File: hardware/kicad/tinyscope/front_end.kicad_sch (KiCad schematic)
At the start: 0 parts

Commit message: feat: hardware: Adds first stage TVS diodes for Front End A/B
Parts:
- added D10, D11: SMAJ48CA, Diode_SMD:D_SMA, symbol Diode:SMAJ48CA
- added J6: Front End A, symbol Connector:Conn_Coaxial
- added J7: Front End B, symbol Connector:Conn_Coaxial
- added R? (x2): 1M, symbol Device:R_Small
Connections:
- new net: D11.2 (A2), J7.1 (In), R?.1
- new net: D10.2 (A2), J6.1 (In), R?.1
- new net GND: D10.1 (A1), D11.1 (A1), J6.2 (Ext), J7.2 (Ext), R?.2, R?.2

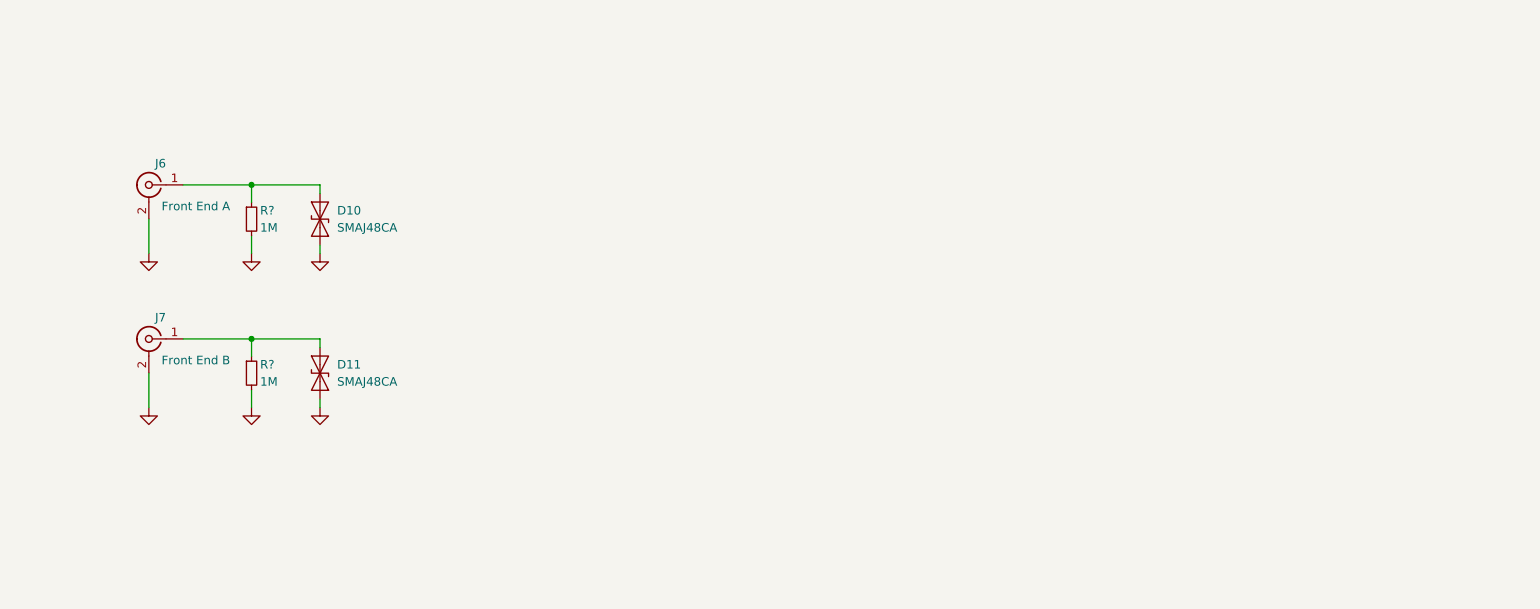
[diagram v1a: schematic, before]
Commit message: feat: hardware: Adds BV199 clamps and AD8065 buffers for Front End A/B
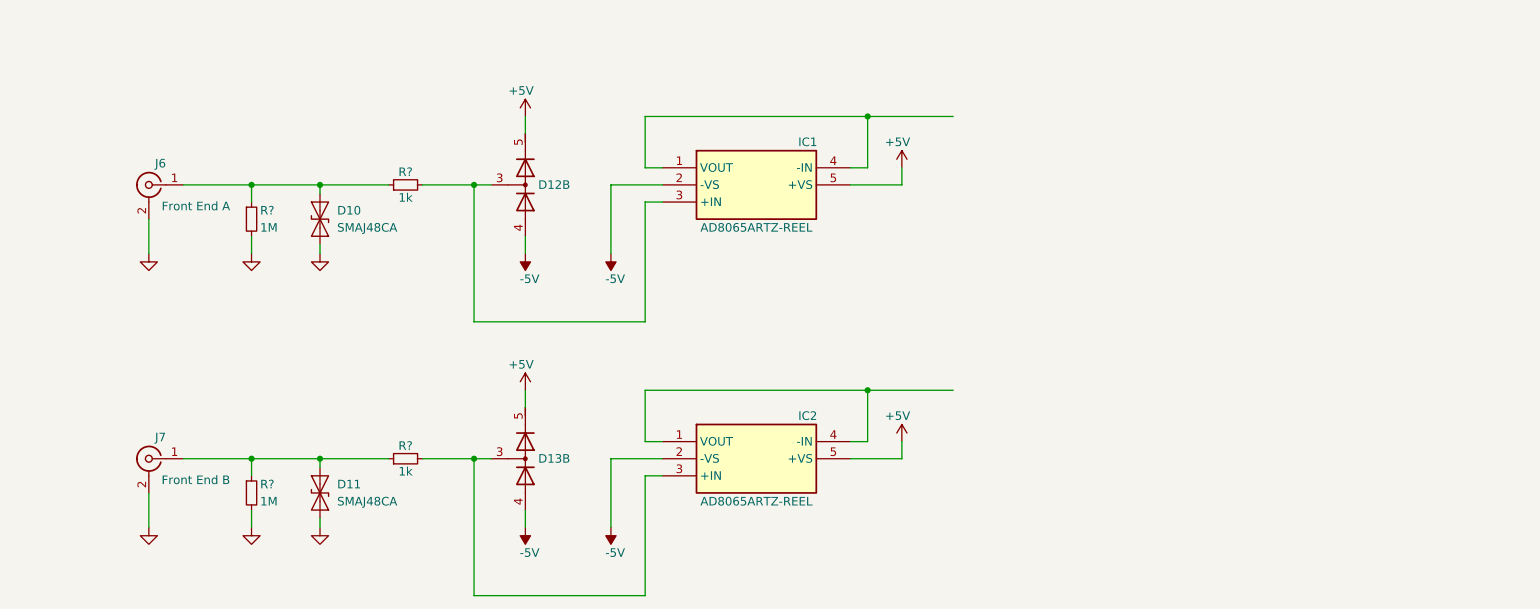
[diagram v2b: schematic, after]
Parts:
- added D12, D13: BAV199DW, Package_TO_SOT_SMD:SOT-363_SC-70-6, symbol Diode:BAV199DW
- added IC1, IC2: AD8065ARTZ-REEL, SOT95P280X145-5N, symbol AD8065ARTZ-REEL:AD8065ARTZ-REEL
- added R? (x2): 1k, symbol Device:R_Small
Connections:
- net at D11.2 (A2), J7.1 (In), R?.1: now also R?.1
- net at D10.2 (A2), J6.1 (In), R?.1: now also R?.1
- new net: D13.3 (K1A2), IC2.3 (+IN), R?.2
- new net: D12.3 (K1A2), IC1.3 (+IN), R?.2
- new net: IC1.1 (VOUT), IC1.4 (-IN)
- new net: IC2.1 (VOUT), IC2.4 (-IN)
- new net +5V: D12.5 (K4), D13.5 (K4), IC1.5 (+VS), IC2.5 (+VS)
- new net -5V: D12.4 (A3), D13.4 (A3), IC1.2 (-VS), IC2.2 (-VS)
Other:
- moved on the sheet: D11, J7, R?

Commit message: feat: hardware: Finishes front ends stage 4
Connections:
- net AD8065_VOUT: now reaches IC1.1 (VOUT), IC1.4 (-IN)
- net AD8065_VOUT: now also IC2.1 (VOUT), IC2.4 (-IN)
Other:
- moved on the sheet: D10, D11, D12B, D13B, IC1, IC2, J6, J7, R?

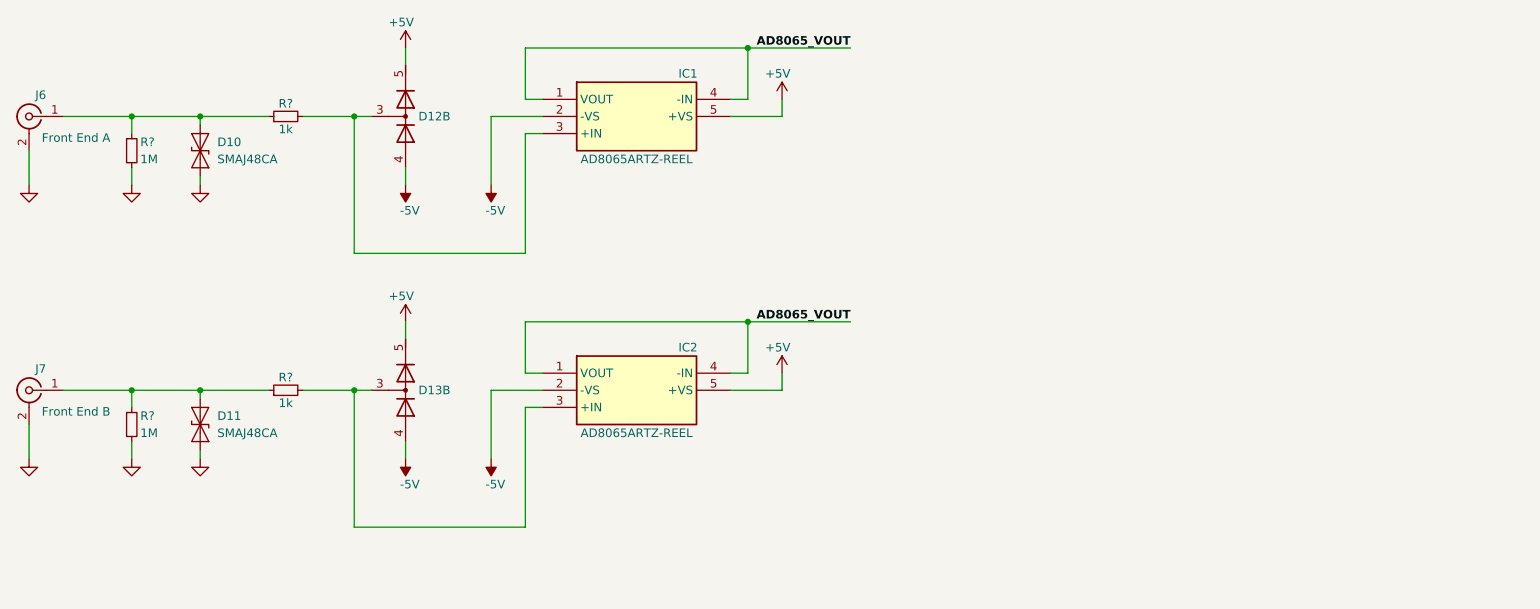
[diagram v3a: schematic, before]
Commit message: feat: hardware: Add front ends stage 5. Replaces AD8065 with AD8066
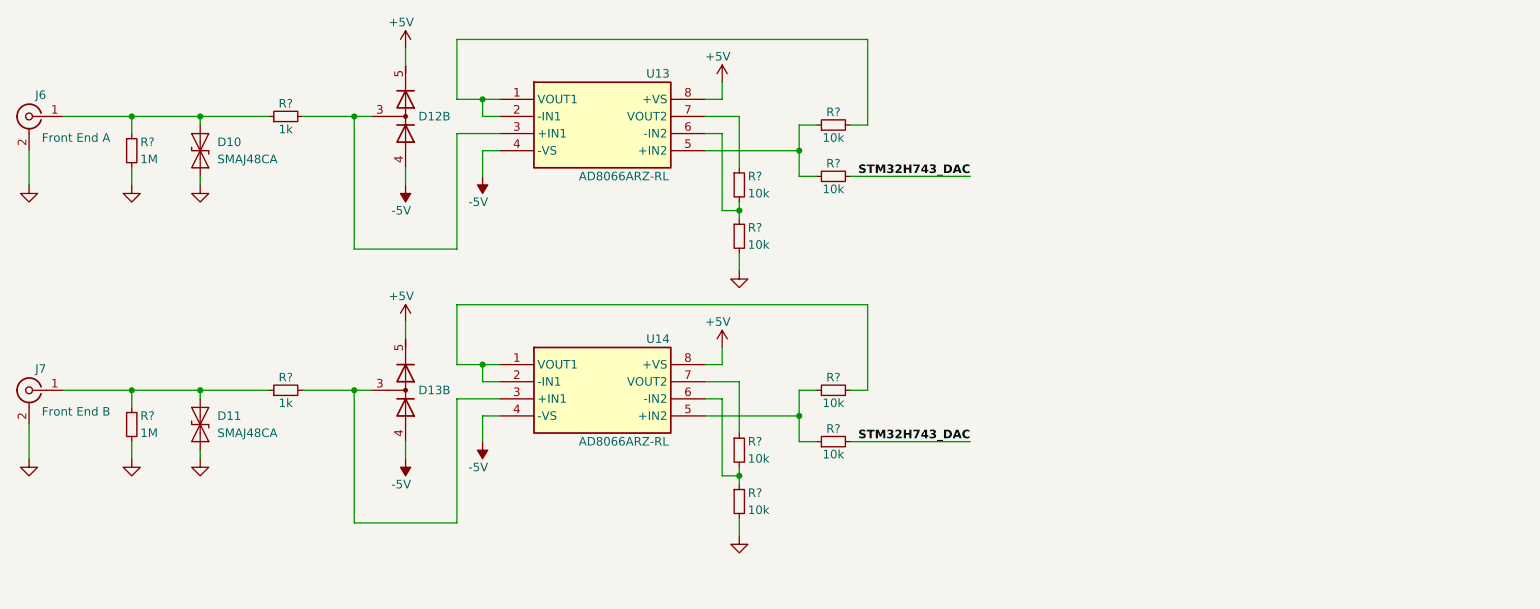
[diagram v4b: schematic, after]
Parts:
- removed IC1, IC2: AD8065ARTZ-REEL, SOT95P280X145-5N, symbol AD8065ARTZ-REEL:AD8065ARTZ-REEL
- added R? (x8): 10k, symbol Device:R_Small
- added U13, U14: AD8066ARZ-RL, SOIC127P600X175-8N, symbol AD8066ARZ-RL:AD8066ARZ-RL
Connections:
- net +5V: now also U13.8 (+VS), U14.8 (+VS)
- net -5V: now also U13.4 (-VS), U14.4 (-VS)
- net GND: now also R?.2, R?.2
- net at D13.3 (K1A2), R?.2: now also U14.3 (+IN1)
- net at D12.3 (K1A2), R?.2: now also U13.3 (+IN1)
- new net: R?.1, U13.7 (VOUT2)
- new net: R?.1, R?.2, U13.6 (-IN2)
- new net: R?.1, U14.7 (VOUT2)
- new net: R?.1, R?.2, U14.6 (-IN2)
- new net: R?.1, R?.1, U13.5 (+IN2)
- new net: R?.1, R?.1, U14.5 (+IN2)
- new net: R?.2, U14.1 (VOUT1), U14.2 (-IN1)
- new net: R?.2, U13.1 (VOUT1), U13.2 (-IN1)
- new net STM32H743_DAC: R?.2, R?.2

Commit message: feat: hardware: Switches SPI1 to SPI4. Adds DAC1_OUT1 and DAC1_OUT2
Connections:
- net STM32H743_DAC renamed STM32H743_DAC1_OUT1
- net STM32H743_DAC1_OUT1: no longer R?.2
- new net STM32H743_DAC1_OUT2: R?.2
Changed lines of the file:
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@@
     (stroke (width 0) (type default))
   )
-  (wire (pts (xy 147.32 39.37) (xy 165.1 39.37))
+  (wire (pts (xy 147.32 39.37) (xy 172.085 39.37))
     (stroke (width 0) (type default))
   )
@@
     (stroke (width 0) (type default))
   )
-  (wire (pts (xy 147.32 78.74) (xy 165.1 78.74))
+  (wire (pts (xy 147.32 78.74) (xy 172.085 78.74))
     (stroke (width 0) (type default))
   )
@@
     (stroke (width 0) (type default))
   )
-  (label "STM32H743_DAC" (at 165.1 39.37 180) (fields_autoplaced)
+  (label "STM32H743_DAC1_OUT1" (at 172.085 39.37 180) (fields_autoplaced)
     (effects (font (size 1.27 1.27) bold) (justify right bottom))
   )
-  (label "STM32H743_DAC" (at 165.1 78.74 180) (fields_autoplaced)
+  (label "STM32H743_DAC1_OUT2" (at 172.085 78.74 180) (fields_autoplaced)
     (effects (font (size 1.27 1.27) bold) (justify right bottom))
   )

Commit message: feat: hardware: note: Starts the desing of the Sallen and Key Low Pass Filter filter (anti-aliasing)
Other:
- note added: "Place for Sallen and Key Low Pass Filter"
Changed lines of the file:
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@@
   (junction (at 92.71 27.94) (diameter 0) (color 0 0 0 0)
   )
+  (junction (at 130.81 30.48) (diameter 0) (color 0 0 0 0)
+  )
   (junction (at 40.64 71.12) (diameter 0) (color 0 0 0 0)
   )
@@
   (junction (at 40.64 30.48) (diameter 0) (color 0 0 0 0)
   )
+  (junction (at 130.81 69.85) (diameter 0) (color 0 0 0 0)
+  )
   (junction (at 139.7 35.56) (diameter 0) (color 0 0 0 0)
   )
@@
     (stroke (width 0) (type default))
   )
+  (wire (pts (xy 130.81 67.31) (xy 172.085 67.31))
+    (stroke (width 0) (type default))
+  )
   (wire (pts (xy 130.81 90.17) (xy 130.81 92.71))
     (stroke (width 0) (type default))
@@
     (stroke (width 0) (type default))
   )
+  (wire (pts (xy 130.81 27.94) (xy 130.81 30.48))
+    (stroke (width 0) (type default))
+  )
   (wire (pts (xy 88.9 58.42) (xy 88.9 67.31))
     (stroke (width 0) (type default))
@@
     (stroke (width 0) (type default))
   )
+  (wire (pts (xy 130.81 67.31) (xy 130.81 69.85))
+    (stroke (width 0) (type default))
+  )
   (wire (pts (xy 142.24 71.12) (xy 139.7 71.12))
     (stroke (width 0) (type default))
@@
     (stroke (width 0) (type default))
   )
+  (wire (pts (xy 130.81 27.94) (xy 172.085 27.94))
+    (stroke (width 0) (type default))
+  )
   (wire (pts (xy 139.7 35.56) (xy 139.7 39.37))
     (stroke (width 0) (type default))
@@
     (stroke (width 0) (type default))
   )
+  (text "Place for Sallen and Key Low Pass Filter" (at 180.975 53.975 0)
+    (effects (font (size 1.27 1.27)) (justify left bottom))
+  )
   (label "STM32H743_DAC1_OUT1" (at 172.085 39.37 180) (fields_autoplaced)

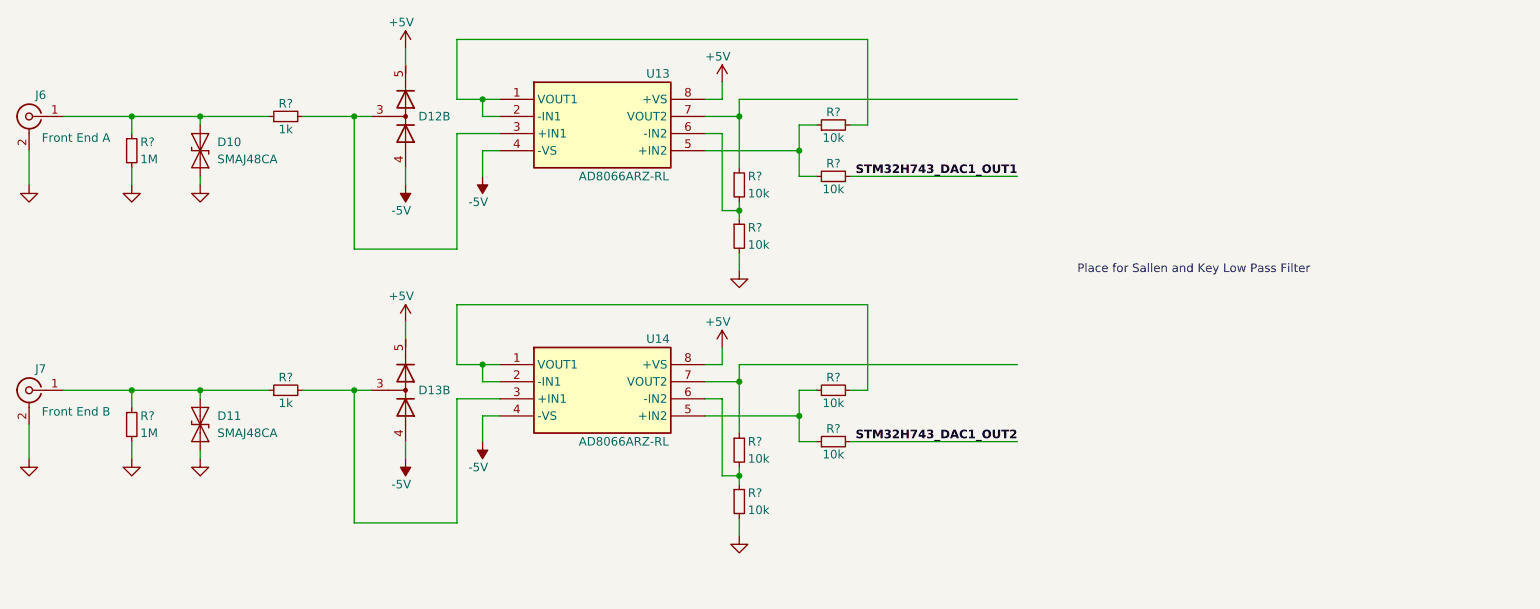
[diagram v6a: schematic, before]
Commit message: feat: hardware: note: Adds the two Sallen and Key Low Pass Filter filter (anti-aliasing) topologies
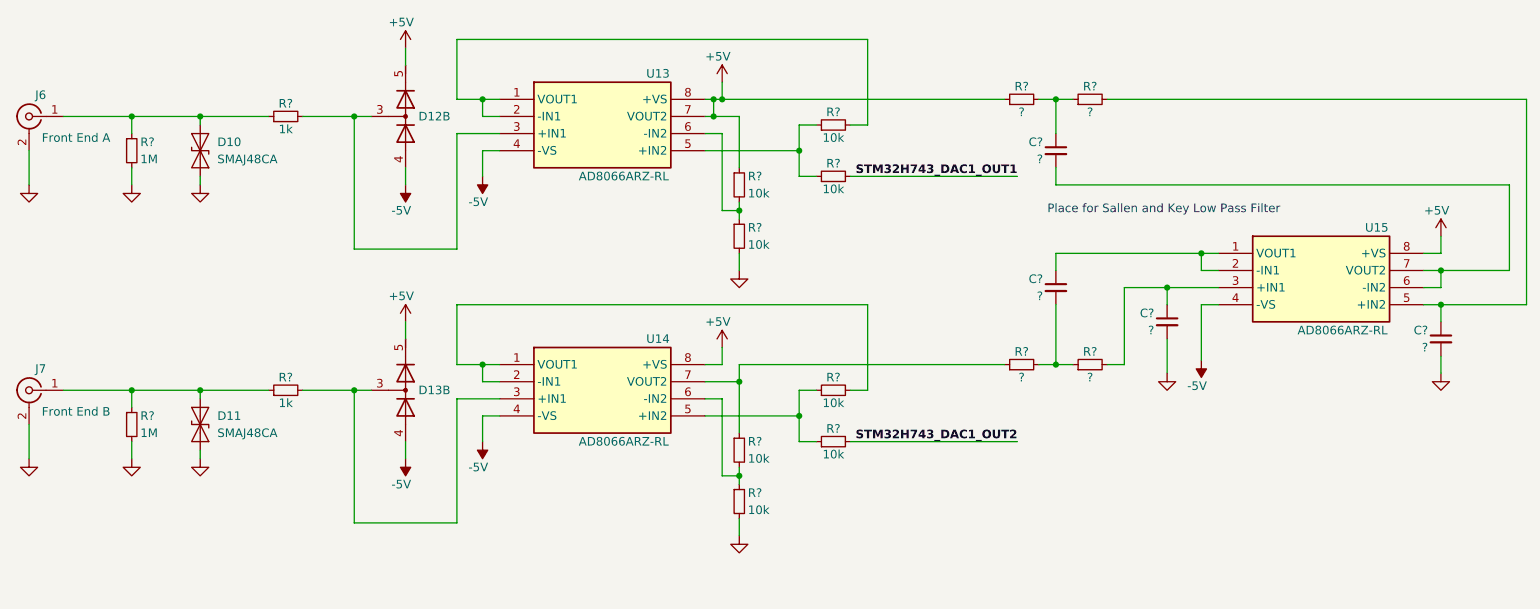
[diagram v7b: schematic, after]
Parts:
- added C? (x4): ?, symbol Device:C_Small
- added R? (x4): ?, symbol Device:R_Small
- added U15: AD8066ARZ-RL, SOIC127P600X175-8N, symbol AD8066ARZ-RL:AD8066ARZ-RL
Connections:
- net +5V: now also R?.1, U13.7 (VOUT2), R?.1, U15.8 (+VS)
- net -5V: now also U15.4 (-VS)
- net GND: now also C?.2, C?.2
- net at R?.1, U14.7 (VOUT2): now also R?.1
- new net: C?.1, R?.2, U15.5 (+IN2)
- new net: C?.1, R?.1, R?.2
- new net: C?.1, U15.1 (VOUT1), U15.2 (-IN1)
- new net: C?.1, R?.2, U15.3 (+IN1)
- new net: C?.2, U15.6 (-IN2), U15.7 (VOUT2)
- new net: C?.2, R?.1, R?.2

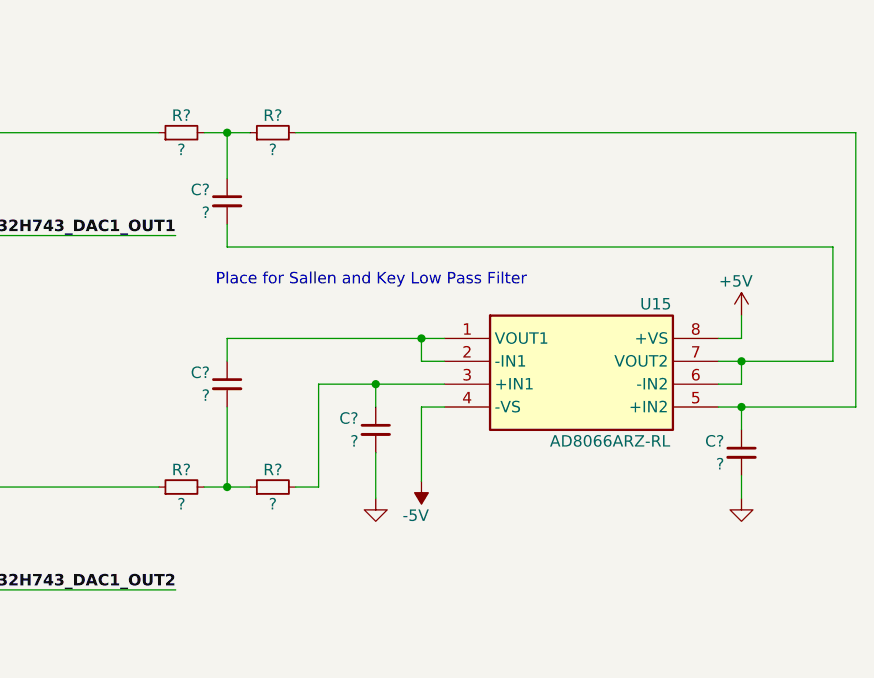
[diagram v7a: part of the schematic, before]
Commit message: feat: hardware: note: Adds the two Sallen and Key Low Pass Filter filter (anti-aliasing) parts values
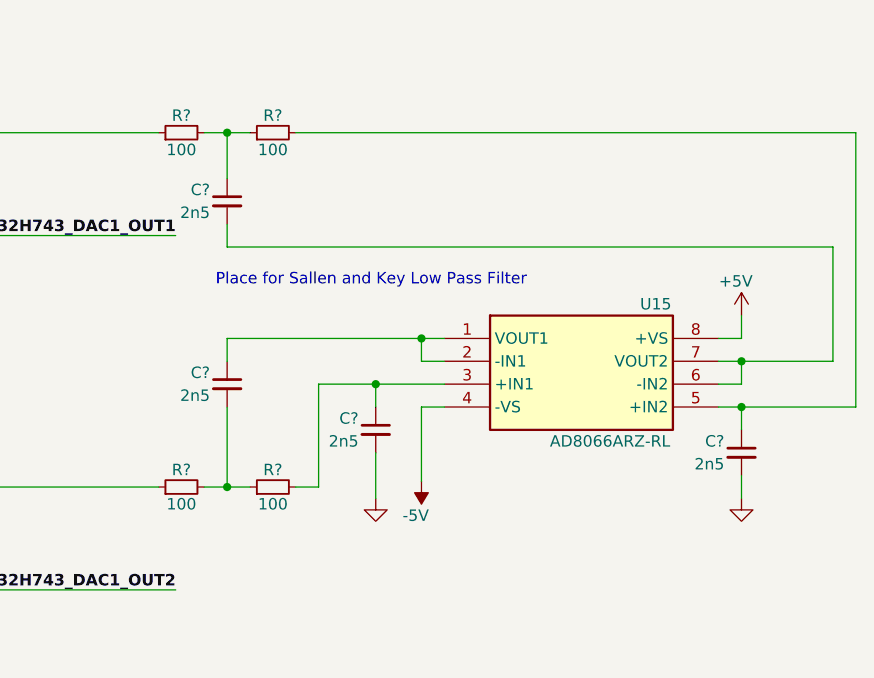
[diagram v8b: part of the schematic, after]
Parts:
- C? (x4): value ? -> 2n5
- R? (x4): value ? -> 100
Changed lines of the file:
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@@
       (effects (font (size 1.27 1.27)) (justify right))
     )
-    (property "Value" "?" (at 233.045 64.77 0)
+    (property "Value" "2n5" (at 233.045 64.77 0)
       (effects (font (size 1.27 1.27)) (justify right))
     )
@@
       (effects (font (size 1.27 1.27)))
     )
-    (property "Value" "?" (at 172.72 29.845 90)
+    (property "Value" "100" (at 172.72 29.845 90)
       (effects (font (size 1.27 1.27)))
     )
@@
       (effects (font (size 1.27 1.27)))
     )
-    (property "Value" "?" (at 182.88 29.845 90)
+    (property "Value" "100" (at 182.88 29.845 90)
       (effects (font (size 1.27 1.27)))
     )
@@
       (effects (font (size 1.27 1.27)))
     )
-    (property "Value" "?" (at 172.72 69.215 90)
+    (property "Value" "100" (at 172.72 69.215 90)
       (effects (font (size 1.27 1.27)))
     )
@@
       (effects (font (size 1.27 1.27)))
     )
-    (property "Value" "?" (at 182.88 69.215 90)
+    (property "Value" "100" (at 182.88 69.215 90)
       (effects (font (size 1.27 1.27)))
     )
@@
       (effects (font (size 1.27 1.27)) (justify right))
     )
-    (property "Value" "?" (at 192.405 62.23 0)
+    (property "Value" "2n5" (at 192.405 62.23 0)
       (effects (font (size 1.27 1.27)) (justify right))
     )
@@
       (effects (font (size 1.27 1.27)) (justify right))
     )
-    (property "Value" "?" (at 175.895 36.83 0)
+    (property "Value" "2n5" (at 175.895 36.83 0)
       (effects (font (size 1.27 1.27)) (justify right))
     )
@@
       (effects (font (size 1.27 1.27)) (justify right))
     )
-    (property "Value" "?" (at 175.895 57.15 0)
+    (property "Value" "2n5" (at 175.895 57.15 0)
       (effects (font (size 1.27 1.27)) (justify right))
     )
